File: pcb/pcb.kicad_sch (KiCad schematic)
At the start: 20 parts, among them J1 Conn_01x03_Pin, J2 Screw_Terminal_01x06, J3 Barrel_Jack_Switch, J5 DE9_Plug, U1 74LS165, U2 LM7805_TO220

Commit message: New PDB files
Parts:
- removed J5: DE9_Plug, Connector_Dsub:DSUB-9_Female_Horizontal_P2.77x2.84mm_EdgePinOffset7.70mm_Housed_MountingHolesOffset9.12mm, symbol Connector:DE9_Plug
- added J4: DE9_Plug_MountingHoles, Connector_Dsub:DSUB-9_Female_Horizontal_P2.77x2.84mm_EdgePinOffset7.70mm_Housed_MountingHolesOffset9.12mm, symbol Connector:DE9_Plug_MountingHoles
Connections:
- net C_CK: now also J4.2
- net C_DATA: now also J4.4
- net C_LA: now also J4.3
- net GND: now also J4.0 (PAD)
- net VIDEO: now also J2.5 (Pin_5); no longer J2.4 (Pin_4)
- net V_SYNC: now also J2.4 (Pin_4); no longer J2.5 (Pin_5)
- net at JP3.2 (B): now also J4.6
- net at JP2.2 (B): now also J4.7
- net at JP4.2 (B): now also J4.8
- net at JP1.2 (B): now also J4.9
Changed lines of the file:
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@@
 	(global_label "V_SYNC"
 		(shape input)
-		(at 60.96 161.29 180)
+		(at 60.96 158.75 180)
 		(fields_autoplaced yes)
 		(effects
@@
 		)
 		(property "Intersheetrefs" "${INTERSHEET_REFS}"
-			(at 51.02 161.29 0)
+			(at 51.02 158.75 0)
 			(effects
 				(font
@@
 	(global_label "VIDEO"
 		(shape input)
-		(at 60.96 158.75 180)
+		(at 60.96 161.29 180)
 		(fields_autoplaced yes)
 		(effects
@@
 		)
 		(property "Intersheetrefs" "${INTERSHEET_REFS}"
-			(at 52.5319 158.75 0)
+			(at 52.5319 161.29 0)
 			(effects
 				(font
@@
 	)
 	(symbol
-		(lib_id "Connector:DE9_Plug")
-		(at 262.89 110.49 0)
-		(unit 1)
-		(exclude_from_sim no)
-		(in_bom yes)
-		(on_board yes)
-		(dnp no)
-		(fields_autoplaced yes)
-		(property "Reference" "J5"
-			(at 267.97 109.2199 0)
-			(effects
-				(font
-					(size 1.27 1.27)
-				)
-				(justify left)
-			)
-		)
-		(property "Value" "DE9_Plug"
-			(at 267.97 111.7599 0)
-			(effects
-				(font
-					(size 1.27 1.27)
-				)
-				(justify left)
-			)
-		)
-		(property "Footprint" "Connector_Dsub:DSUB-9_Female_Horizontal_P2.77x2.84mm_EdgePinOffset7.70mm_Housed_MountingHolesOffset9.12mm"
-			(at 262.89 110.49 0)
-			(effects
-				(font
-					(size 1.27 1.27)
-				)
-				(hide yes)
-			)
-		)
-		(property "Datasheet" "~"
-			(at 262.89 110.49 0)
-			(effects
-				(font
-					(size 1.27 1.27)
-				)
-				(hide yes)
-			)
-		)
-		(property "Description" "9-pin male plug pin D-SUB connector"
-			(at 262.89 110.49 0)
-			(effects
-				(font
-					(size 1.27 1.27)
-				)
-				(hide yes)
-			)
-		)
-		(pin "8"
-		)
-		(pin "9"
-		)
-		(pin "1"
-		)
-		(pin "3"
-		)
-		(pin "5"
-		)
-		(pin "7"
-		)
-		(pin "2"
-		)
-		(pin "4"
-		)
-		(pin "6"
-		)
-		(instances
-			(project ""
-				(path "/e222e52e-83a8-4556-a94e-a22482ba41c4"
-					(reference "J5")
-					(unit 1)
-				)
-			)
-		)
-	)
-	(symbol
 		(lib_id "power:GND")
 		(at 233.68 113.03 0)
@@
 	)
 	(symbol
+		(lib_id "Connector:DE9_Plug_MountingHoles")
+		(at 262.89 110.49 0)
+		(unit 1)
+		(exclude_from_sim no)
+		(in_bom yes)
+		(on_board yes)
+		(dnp no)
+		(fields_autoplaced yes)
+		(property "Reference" "J4"
+			(at 267.97 109.2199 0)
+			(effects
+				(font
+					(size 1.27 1.27)
+				)
+				(justify left)
+			)
+		)
+		(property "Value" "DE9_Plug_MountingHoles"
+			(at 267.97 111.7599 0)
+			(effects
+				(font
+					(size 1.27 1.27)
+				)
+				(justify left)
+			)
+		)
+		(property "Footprint" "Connector_Dsub:DSUB-9_Female_Horizontal_P2.77x2.84mm_EdgePinOffset7.70mm_Housed_MountingHolesOffset9.12mm"
+			(at 262.89 110.49 0)
+			(effects
+				(font
+					(size 1.27 1.27)
+				)
+				(hide yes)
+			)
+		)
+		(property "Datasheet" "~"
+			(at 262.89 110.49 0)
+			(effects
+				(font
+					(size 1.27 1.27)
+				)
+				(hide yes)
+			)
+		)
+		(property "Description" "9-pin male plug pin D-SUB connector, Mounting Hole"
+			(at 262.89 110.49 0)
+			(effects
+				(font
+					(size 1.27 1.27)
+				)
+				(hide yes)
+			)
+		)
+		(pin "8"
+		)
+		(pin "0"
+		)
+		(pin "9"
+		)
+		(pin "4"
+		)
+		(pin "6"
+		)
+		(pin "7"
+		)
+		(pin "3"
+		)
+		(pin "5"
+		)
+		(pin "1"
+		)
+		(pin "2"
+		)
+		(instances
+			(project ""
+				(path "/e222e52e-83a8-4556-a94e-a22482ba41c4"
+					(reference "J4")
+					(unit 1)
+				)
+			)
+		)
+	)
+	(symbol
 		(lib_id "power:GND")
 		(at 45.72 80.01 0)
@@
 					(unit 1)
 				)
+			)
+		)
+	)
+	(symbol
+		(lib_id "power:GND")
+		(at 262.89 125.73 0)
+		(unit 1)
+		(exclude_from_sim no)
+		(in_bom yes)
+		(on_board yes)
+		(dnp no)
+		(fields_autoplaced yes)
+		(property "Reference" "#PWR022"
+			(at 262.89 132.08 0)
+			(effects
+				(font
+					(size 1.27 1.27)
+				)
+				(hide yes)
+			)
+		)
+		(property "Value" "GND"
+			(at 262.89 130.81 0)
+			(effects
+				(font
+					(size 1.27 1.27)
+				)
+			)
+		)
+		(property "Footprint" ""
+			(at 262.89 125.73 0)
+			(effects
+				(font
+					(size 1.27 1.27)
+				)
+				(hide yes)
+			)
+		)
+		(property "Datasheet" ""
+			(at 262.89 125.73 0)
+			(effects
+				(font
+					(size 1.27 1.27)
+				)
+				(hide yes)
+			)
+		)
+		(property "Description" "Power symbol creates a global label with name \"GND\" , ground"
+			(at 262.89 125.73 0)
+			(effects
+				(font
+					(size 1.27 1.27)
+				)
+				(hide yes)
+			)
+		)
+		(pin "1"
+		)
+		(instances
+			(project "pcb"
+				(path "/e222e52e-83a8-4556-a94e-a22482ba41c4"
+					(reference "#PWR022")
+					(unit 1)
+				)

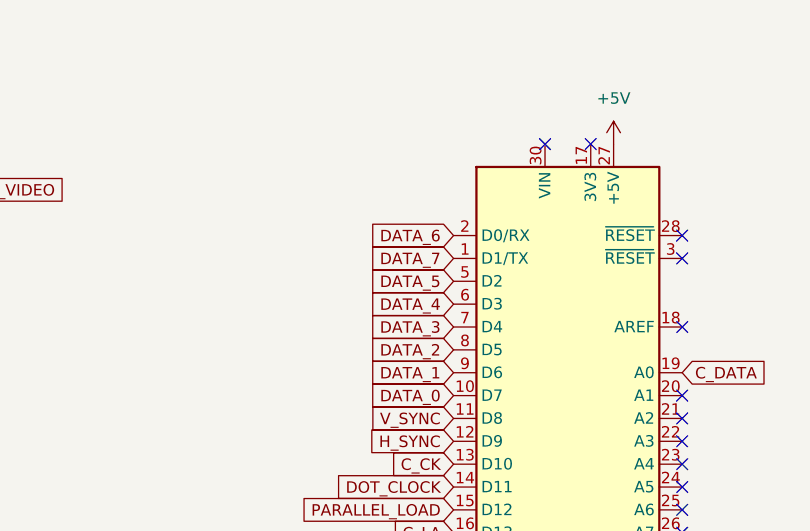
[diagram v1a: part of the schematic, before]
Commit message: Fix backwards data lines
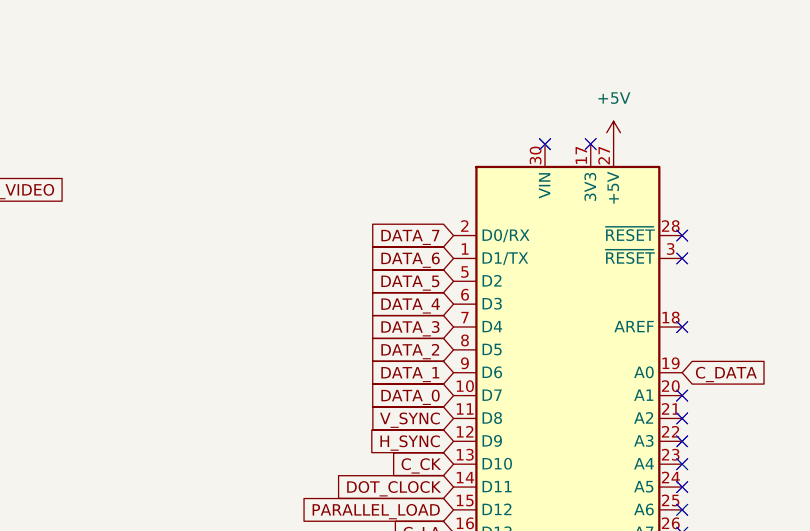
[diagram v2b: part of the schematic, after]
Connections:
- net DATA_6: now also A1.1 (D1/TX); no longer A1.2 (D0/RX)
- net DATA_7: now also A1.2 (D0/RX); no longer A1.1 (D1/TX)
